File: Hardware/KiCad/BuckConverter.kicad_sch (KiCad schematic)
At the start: 12 parts, among them U1 TPS56339DDC

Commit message: revB
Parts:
- removed C1: 10u, Capacitor_SMD:C_0805_2012Metric_Pad1.18x1.45mm_HandSolder, symbol Device:C
- removed C16, C2: 100n, Capacitor_SMD:C_0603_1608Metric_Pad1.08x0.95mm_HandSolder, symbol Device:C
- removed C17, C18, C3: 22u, Capacitor_SMD:C_0805_2012Metric_Pad1.18x1.45mm_HandSolder, symbol Device:C
- removed L1: 6.8u, Inductor_SMD:L_6.3x6.3_H3, symbol Device:L
- removed R1: 30, Resistor_SMD:R_0603_1608Metric_Pad0.98x0.95mm_HandSolder, symbol Device:R
- removed R16: 220k, Resistor_SMD:R_0603_1608Metric_Pad0.98x0.95mm_HandSolder, symbol Device:R
- removed R2: 140k, Resistor_SMD:R_0603_1608Metric_Pad0.98x0.95mm_HandSolder, symbol Device:R
- removed R9: 10k, Resistor_SMD:R_0603_1608Metric_Pad0.98x0.95mm_HandSolder, symbol Device:R
- removed U1: TPS56339DDC, Package_TO_SOT_SMD:SOT-23-6, symbol Regulator_Switching:TPS56339DDC
- added C1: 10u, Capacitor_SMD:C_0805_2012Metric_Pad1.18x1.45mm_HandSolder, symbol Device:C_Small
- added C16: 100n, Capacitor_SMD:C_0603_1608Metric_Pad1.08x0.95mm_HandSolder, symbol Device:C_Small
- added C17, C18, C19, C22: 22u, Capacitor_SMD:C_0805_2012Metric_Pad1.18x1.45mm_HandSolder, symbol Device:C_Small
- added C2: 220n, Capacitor_SMD:C_0603_1608Metric_Pad1.08x0.95mm_HandSolder, symbol Device:C_Small
- added C3: 1u, Capacitor_SMD:C_0603_1608Metric_Pad1.08x0.95mm_HandSolder, symbol Device:C_Small
- added L1: 27u, symbol Device:L_Small
- added R1: 100k, Resistor_SMD:R_0603_1608Metric_Pad0.98x0.95mm_HandSolder, symbol Device:R_Small
- added R2: 9.09k, Resistor_SMD:R_0603_1608Metric_Pad0.98x0.95mm_HandSolder, symbol Device:R_Small
- added U1: LMR33610ADDAR, Package_SO:Texas_HSOP-8-1EP_3.9x4.9mm_P1.27mm_ThermalVias, symbol Regulator_Switching:LMR33610ADDAR
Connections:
- net +24V: now also C1.1, C2.1, U1.2 (VIN), U1.3 (EN)
- net 12V_BUS: now also C17.1, C18.1, C19.1, C22.1, L1.2, R1.1
- net GND: now also C1.2, C17.2, C18.2, C19.2, C2.2, C22.2, C3.2, R2.2, U1.1 (GND), U1.9 (GND)
- new net: R1.2, R2.1, U1.5 (FB)
- new net: C16.2, L1.1, U1.8 (SW)
- new net: C16.1, U1.7 (BOOT)
- new net: C3.1, U1.6 (VCC)
- no-connect marks 0 -> 1

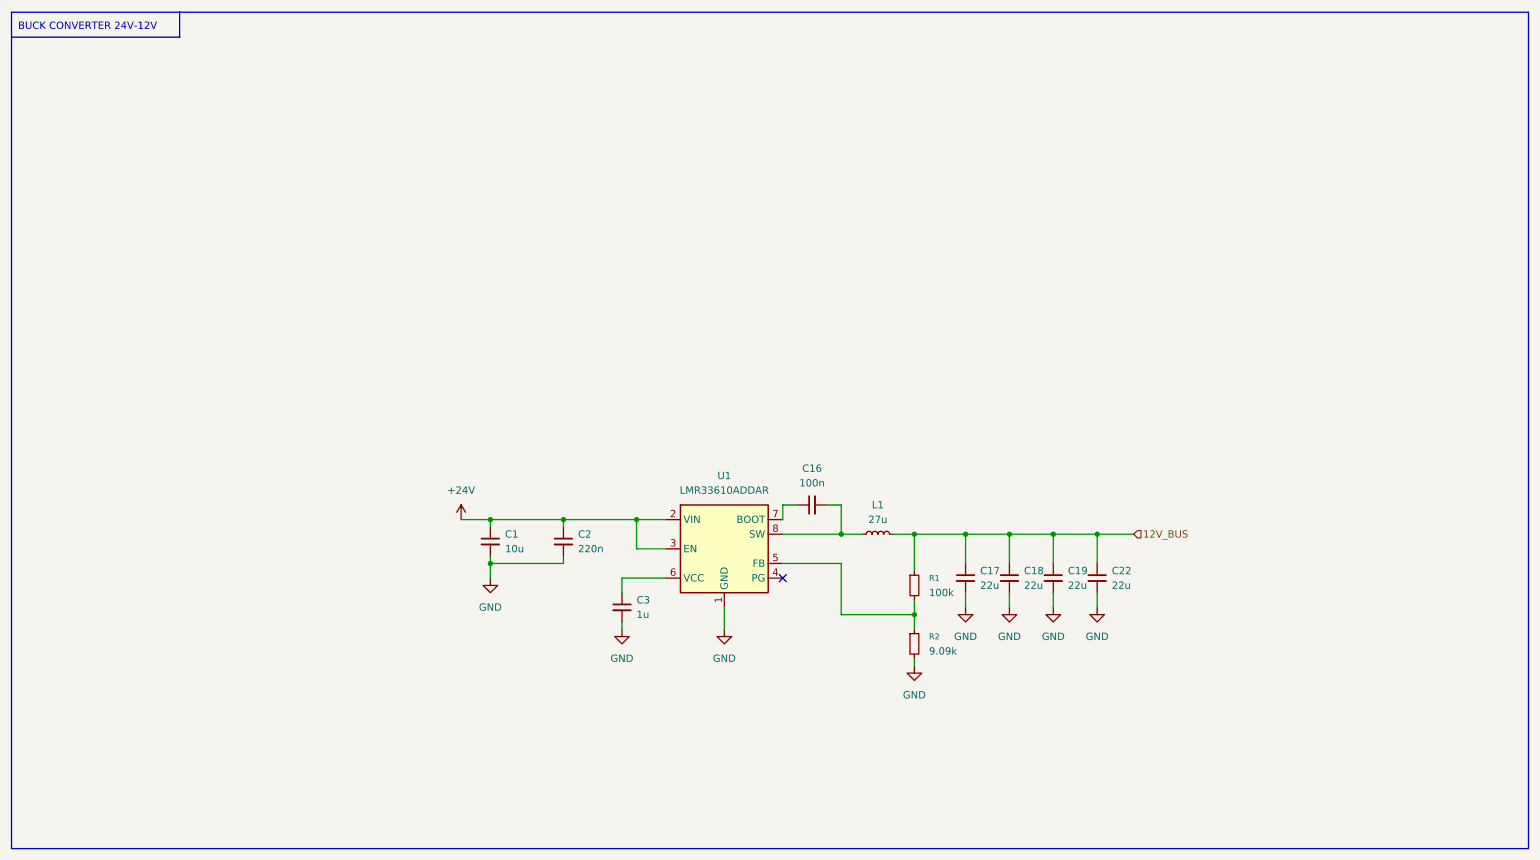
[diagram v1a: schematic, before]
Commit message: schematic changes, pre pcb revB changes
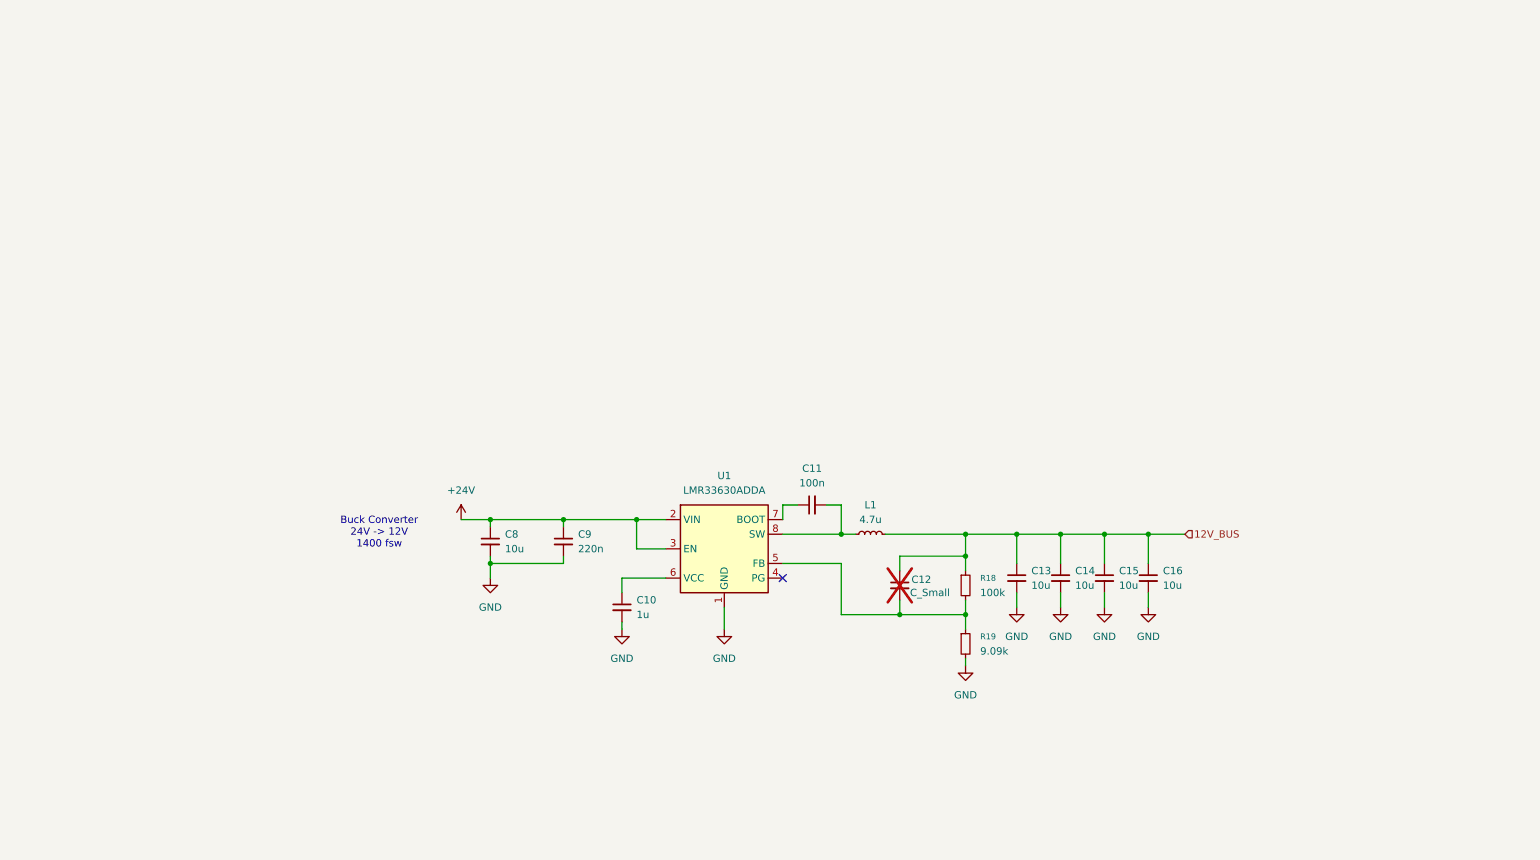
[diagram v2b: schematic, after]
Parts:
- removed U1: LMR33610ADDAR, Package_SO:Texas_HSOP-8-1EP_3.9x4.9mm_P1.27mm_ThermalVias, symbol Regulator_Switching:LMR33610ADDAR
- added C12: C_Small, Capacitor_SMD:C_0603_1608Metric_Pad1.08x0.95mm_HandSolder, symbol Device:C_Small
- added U1: LMR33630ADDA, Package_SO:Texas_HSOP-8-1EP_3.9x4.9mm_P1.27mm_ThermalVias, symbol Regulator_Switching:LMR33630ADDA
- C10: renamed from C3; LCSC (none) -> C15849
- C11: renamed from C16; LCSC (none) -> C14663
- C13: renamed from C17; value 22u -> 10u; LCSC (none) -> C440198
- C14: renamed from C18; value 22u -> 10u; LCSC (none) -> C440198
- C15: renamed from C19; value 22u -> 10u; LCSC (none) -> C440198
- C16: renamed from C22; value 22u -> 10u; LCSC (none) -> C440198
- C8: renamed from C1; LCSC (none) -> C440198
- C9: renamed from C2; LCSC (none) -> C344195
- L1: value 27u -> 4.7u; footprint (none) -> easyeda2kicad:IND-SMD_L5.0-W5.0
- R18: renamed from R1; LCSC (none) -> C25803
- renumbered R2 to R19
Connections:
- net +24V: now also U1.2 (VIN), U1.3 (EN)
- net 12V_BUS: now also C12.1
- net GND: now also U1.1 (GND), U1.9 (GND)
- net at R18.2, R19.1: now also C12.2, U1.5 (FB)
- net at C11.2, L1.1: now also U1.8 (SW)
- net at C11.1: now also U1.7 (BOOT)
- net at C10.1: now also U1.6 (VCC)
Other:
- note added: "Buck Converter 24V -> 12V 1400 fsw"
- note removed: "BUCK CONVERTER 24V-12V"
- moved on the sheet: C13, C14, C15, C16, L1, R18, R19

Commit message: sch changes, pre pcb changes
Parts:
- added R17: 100k, Resistor_SMD:R_0603_1608Metric_Pad0.98x0.95mm_HandSolder, symbol Device:R_Small
- added R18: 9.09k, Resistor_SMD:R_0603_1608Metric_Pad0.98x0.95mm_HandSolder, symbol Device:R_Small
- renumbered R18 to R15, R19 to R16
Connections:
- net 12V_BUS: now also R17.1
- net GND: now also R18.2
- net +24V renamed 24VIN
- new net 12V_SENSE: R17.2, R18.1
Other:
- note added: "12V_Sense = 12V_BUS*(R_Bottom)/(R_Top + T_Bottom) 12V_Sense = 12*(100k)/(100k + 9.09k) 12V_Sense = 1.0V"
- moved on the sheet: C10, C11, C12, C13, C14, C15, C16, C8, C9, L1, R15, R16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

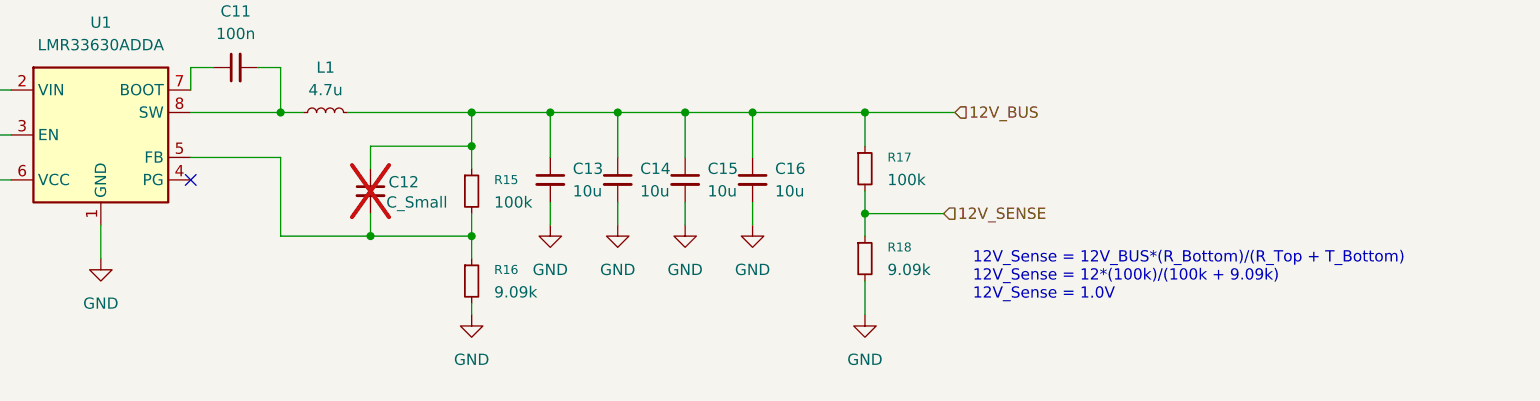
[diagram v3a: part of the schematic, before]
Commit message: layout ready for review
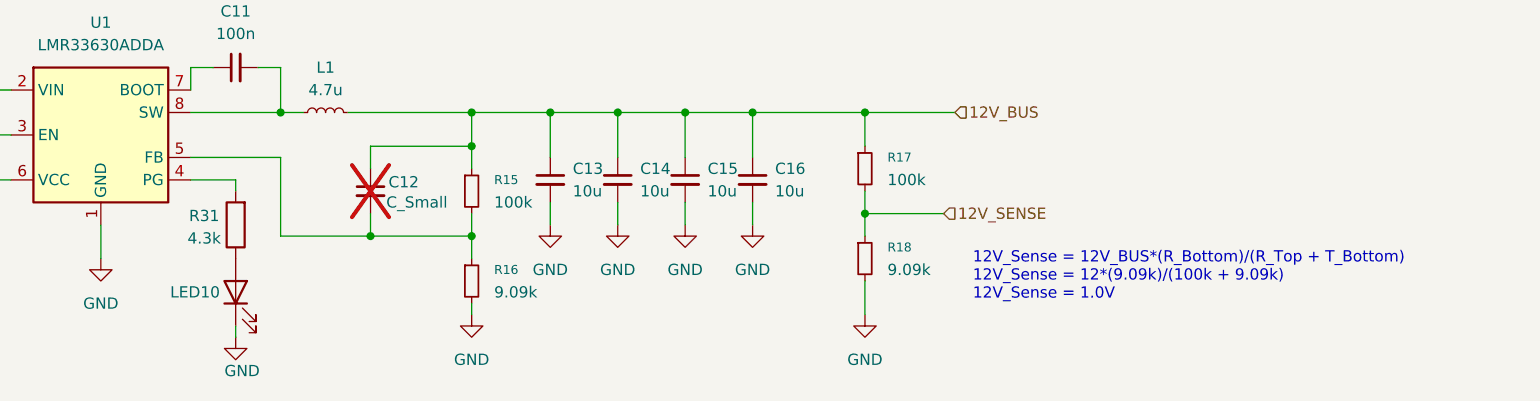
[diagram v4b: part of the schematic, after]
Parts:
- added LED10: LED, LED_SMD:LED_0603_1608Metric, symbol Device:LED
- added R31: 4.3k, Resistor_SMD:R_0603_1608Metric_Pad0.98x0.95mm_HandSolder, symbol Device:R
- C13, C14, C15, C16, C8: footprint Capacitor_SMD:C_0805_2012Metric_Pad1.18x1.45mm_HandSolder -> Capacitor_SMD:C_0603_1608Metric_Pad1.08x0.95mm_HandSolder
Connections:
- net GND: now also LED10.1 (K)
- net at U1.4 (PG): now also R31.2
- new net: LED10.2 (A), R31.1
- no-connect marks 1 -> 0
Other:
- note added: "12V_Sense = 12V_BUS*(R_Bottom)/(R_Top + T_Bottom) 12V_Sense = 12*(9.09k)/(100k + 9.09k) 12V_Sense = 1.0V"
- note removed: "12V_Sense = 12V_BUS*(R_Bottom)/(R_Top + T_Bottom) 12V_Sense = 12*(100k)/(100k + 9.09k) 12V_Sense = 1.0V"

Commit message: layout done
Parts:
- added TP4: TP_PG, TestPoint:TestPoint_Pin_1.0x1.0mm, symbol Connector:TestPoint
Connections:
- net at R31.2, U1.4 (PG): now also TP4.1
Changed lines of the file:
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@@
 	)
 	(junction
+		(at 130.81 114.3)
+		(diameter 0)
+		(color 0 0 0 0)
+	)
+	(junction
 		(at 146.05 120.65)
 		(diameter 0)
@@
 					(unit 1)
 				)
+			)
+		)
+	)
+	(symbol
+		(lib_id "Connector:TestPoint")
+		(at 130.81 114.3 270)
+		(unit 1)
+		(exclude_from_sim no)
+		(in_bom no)
+		(on_board yes)
+		(dnp no)
+		(property "Reference" "TP4"
+			(at 135.128 113.284 0)
+			(effects
+				(font
+					(size 1.27 1.27)
+				)
+				(justify right)
+			)
+		)
+		(property "Value" "TP_PG"
+			(at 132.588 113.284 0)
+			(effects
+				(font
+					(size 1.27 1.27)
+				)
+				(justify right)
+			)
+		)
+		(property "Footprint" "TestPoint:TestPoint_Pin_1.0x1.0mm"
+			(at 130.81 119.38 0)
+			(effects
+				(font
+					(size 1.27 1.27)
+				)
+				(hide yes)
+			)
+		)
+		(property "Datasheet" "~"
+			(at 130.81 119.38 0)
+			(effects
+				(font
+					(size 1.27 1.27)
+				)
+				(hide yes)
+			)
+		)
+		(property "Description" "test point"
+			(at 130.81 114.3 0)
+			(effects
+				(font
+					(size 1.27 1.27)
+				)
+				(hide yes)
+			)
+		)
+		(property "Manufacturer" ""
+			(at 130.81 114.3 0)
+			(effects
+				(font
+					(size 1.27 1.27)
+				)
+				(hide yes)
+			)
+		)
+		(property "Mouser Link" ""
+			(at 130.81 114.3 0)
+			(effects
+				(font
+					(size 1.27 1.27)
+				)
+				(hide yes)
+			)
+		)
+		(property "Sim.Type" ""
+			(at 130.81 114.3 0)
+			(effects
+				(font
+					(size 1.27 1.27)
+				)
+				(hide yes)
+			)
+		)
+		(property "Description (Customer #)" ""
+			(at 130.81 114.3 0)
+			(effects
+				(font
+					(size 1.27 1.27)
+				)
+				(hide yes)
+			)
+		)
+		(property "LCSC" ""
+			(at 130.81 114.3 0)
+			(effects
+				(font
+					(size 1.27 1.27)
+				)
+				(hide yes)
+			)
+		)
+		(pin "1"
+		)
+		(instances
+			(project "PS-MotorControllerInterfacePCB"
+				(path "/a2e13c19-ff3a-4e43-a7f5-200fd5b2b978/2c6af1c6-af26-4746-8ed9-5deb88ce0ee1"
+					(reference "TP4")
+					(unit 1)
+				)

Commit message: done with changes
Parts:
- BUCK_PG1: renamed from TP4; footprint TestPoint:TestPoint_Pin_1.0x1.0mm -> TestPoint:TestPoint_Keystone_5000-5004_Miniature; now in the parts list
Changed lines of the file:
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@@
 	)
 	(hierarchical_label "12V_SENSE"
-		(shape input)
+		(shape output)
 		(at 210.82 118.11 0)
 		(effects
@@
 		(unit 1)
 		(exclude_from_sim no)
-		(in_bom no)
-		(on_board yes)
-		(dnp no)
-		(property "Reference" "TP4"
+		(in_bom yes)
+		(on_board yes)
+		(dnp no)
+		(property "Reference" "BUCK_PG1"
 			(at 135.128 113.284 0)
 			(effects
@@
 			)
 		)
-		(property "Footprint" "TestPoint:TestPoint_Pin_1.0x1.0mm"
+		(property "Footprint" "TestPoint:TestPoint_Keystone_5000-5004_Miniature"
 			(at 130.81 119.38 0)
 			(effects
@@
 			(project "PS-MotorControllerInterfacePCB"
 				(path "/a2e13c19-ff3a-4e43-a7f5-200fd5b2b978/2c6af1c6-af26-4746-8ed9-5deb88ce0ee1"
-					(reference "TP4")
-					(unit 1)
-				)
+					(reference "BUCK_PG1")
+					(unit 1)
+				)

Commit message: finished LCSC
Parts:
- BUCK_PG1, R16: now left out of the parts list
- C13, C14, C15, C16, C8: LCSC C440198 -> C1691
- L1: LCSC (none) -> C354606
- LED10: LCSC (none) -> C7371904
- R18: LCSC C25803 -> (none); now left out of the parts list
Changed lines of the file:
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@@
 		(unit 1)
 		(exclude_from_sim no)
-		(in_bom yes)
+		(in_bom no)
 		(on_board yes)
 		(dnp no)
@@
 			)
 		)
-		(property "LCSC" ""
+		(property "LCSC" "C354606"
 			(at 140.97 106.68 90)
 			(effects
@@
 		(unit 1)
 		(exclude_from_sim no)
-		(in_bom yes)
+		(in_bom no)
 		(on_board yes)
 		(dnp no)
@@
 			)
 		)
-		(property "LCSC" "C25803"
+		(property "LCSC" ""
 			(at 201.93 123.19 0)
 			(effects
@@
 			)
 		)
-		(property "LCSC" "C440198"
+		(property "LCSC" "C1691"
 			(at 189.23 114.3 0)
 			(effects
@@
 			)
 		)
-		(property "LCSC" "C440198"
+		(property "LCSC" "C1691"
 			(at 173.99 114.3 0)
 			(effects
@@
 			)
 		)
-		(property "LCSC" "C440198"
+		(property "LCSC" "C1691"
 			(at 181.61 114.3 0)
 			(effects
@@
 			)
 		)
-		(property "LCSC" "C440198"
+		(property "LCSC" "C1691"
 			(at 74.93 107.95 0)
 			(effects
@@
 			)
 		)
-		(property "LCSC" ""
+		(property "LCSC" "C7371904"
 			(at 130.81 127 90)
 			(effects
@@
 		(unit 1)
 		(exclude_from_sim no)
-		(in_bom yes)
+		(in_bom no)
 		(on_board yes)
 		(dnp no)
@@
 			)
 		)
-		(property "LCSC" "C440198"
+		(property "LCSC" "C1691"
 			(at 166.37 114.3 0)
 			(effects

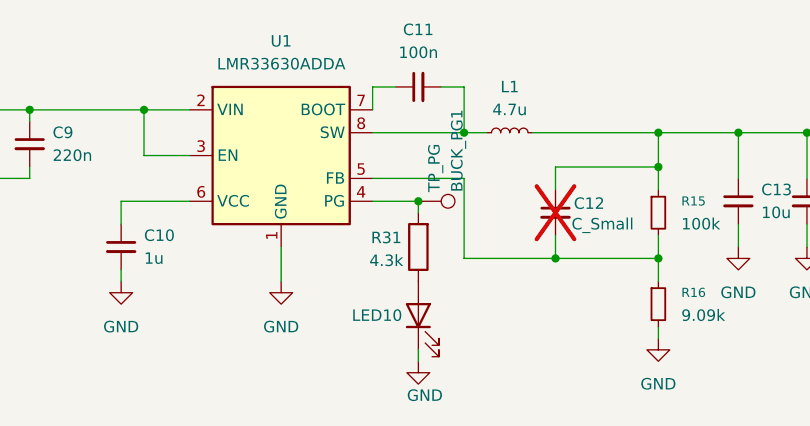
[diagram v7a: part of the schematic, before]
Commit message: fixed references and changed the labels
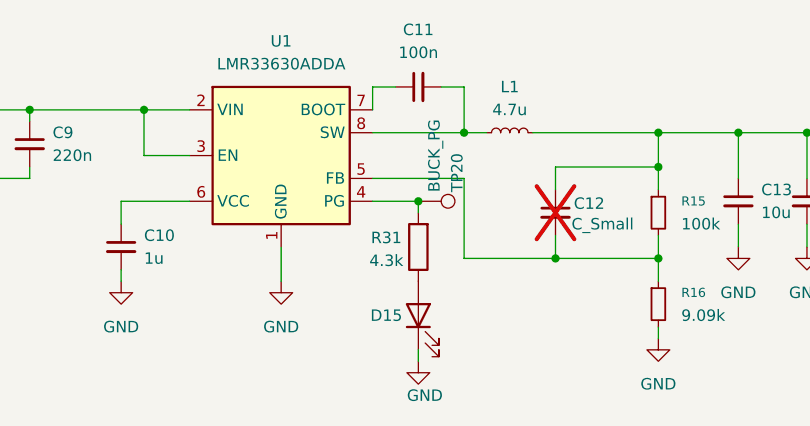
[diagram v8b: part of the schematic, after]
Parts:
- TP20: renamed from BUCK_PG1; value TP_PG -> BUCK_PG
- renumbered LED10 to D15
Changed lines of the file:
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@@
 		(on_board yes)
 		(dnp no)
-		(property "Reference" "LED10"
+		(property "Reference" "D15"
 			(at 129.032 127 90)
 			(effects
@@
 			(project "PS-MotorControllerInterfacePCB"
 				(path "/a2e13c19-ff3a-4e43-a7f5-200fd5b2b978/2c6af1c6-af26-4746-8ed9-5deb88ce0ee1"
-					(reference "LED10")
+					(reference "D15")
 					(unit 1)
 				)
@@
 		(on_board yes)
 		(dnp no)
-		(property "Reference" "BUCK_PG1"
+		(property "Reference" "TP20"
 			(at 135.128 113.284 0)
 			(effects
@@
 			)
 		)
-		(property "Value" "TP_PG"
+		(property "Value" "BUCK_PG"
 			(at 132.588 113.284 0)
 			(effects
@@
 			(project "PS-MotorControllerInterfacePCB"
 				(path "/a2e13c19-ff3a-4e43-a7f5-200fd5b2b978/2c6af1c6-af26-4746-8ed9-5deb88ce0ee1"
-					(reference "BUCK_PG1")
+					(reference "TP20")
 					(unit 1)
 				)
